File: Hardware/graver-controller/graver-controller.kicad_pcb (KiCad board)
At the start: 4 copper layers, 85 x 60 mm, 117 parts, among them J101 Power in 2p, J201 Handpiece pads 1x4, J301 USB-C, J302 SWD, J401 LCD pads 1x7, J402 Pedal pads 1x4, J403 Encoder pads 1x4, Q101 DMP6023LE, Q201 IRLR3410, Q202 SI2309CDS, Q203 BSS123, SW301 BOOT0, SW302 RESET, U101 LM5164DDAR, U102 AP2112K-3.3, U201 UCC27517DBVR, U202 TLV9062IDR, U301 STM32F411CEU6, U302 USBLC6-2SC6, U401 PESD5V0S2BT, Y301 25MHz 10pF

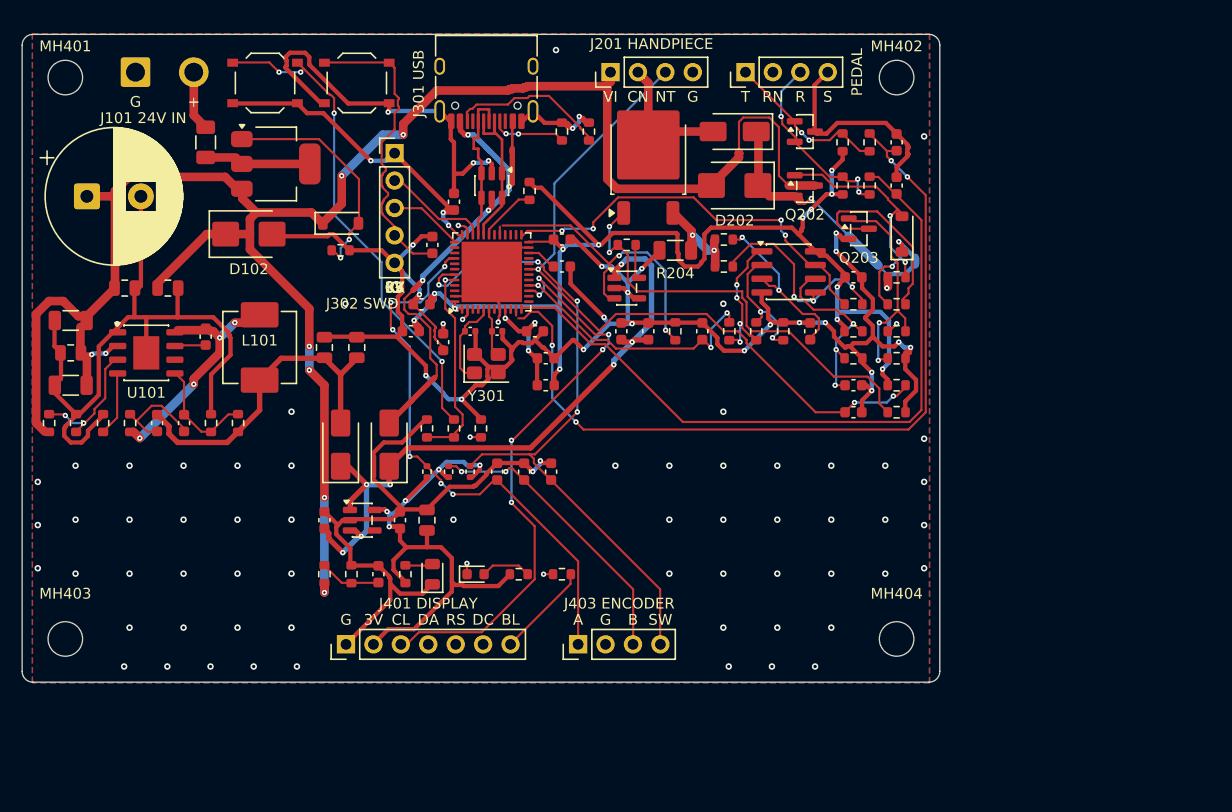
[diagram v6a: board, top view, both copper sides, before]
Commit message: pcb: ADR 0005 accepted - 4-layer board routed, DRC 0/0/0, fab set
kicad-cli DRC after a zone refill: 0 errors, 0 unconnected, 0 schematic
parity, 11 warnings (10 silk_overlap, 1 track_dangling). 85.0 x 60.0 mm.
USB pair 0.25/0.15 with 0.000 mm skew, 0 vias, F.Cu only. Two via sizes,
five track widths, In1/In2 track-free solid planes, every ADR 0003
placement rule met (tools/pcb5/check.py: 0 FAIL).

What it took beyond stage 2: a staggered stub-and-via escape for every
used QFN pin (handroute.py qfn_fan), KRT run with net class clearances and
the hand routes kept, widths snapped to the ADR set (widen.py), plane-tap
vias removed from SMD pads (postroute.py), and explicit joins for the five
pairs the router left open (joins.py: NRST under the QFN, VDDA, the LDO
input, PEDAL_TIP, a GND island). The CLAMP gate-bias branch may use signal
widths (rule area 'clamp-bias' + .kicad_dru), QFN pads need one pour spoke.

Renders in output/pcb/, JLC Gerbers/drill/BOM/CPL in fab/ with a package
convention rotation table to confirm in JLC's preview. ADR 0005 marked
Accepted with the measured numbers; HANDOFF.md points at the new pipeline.
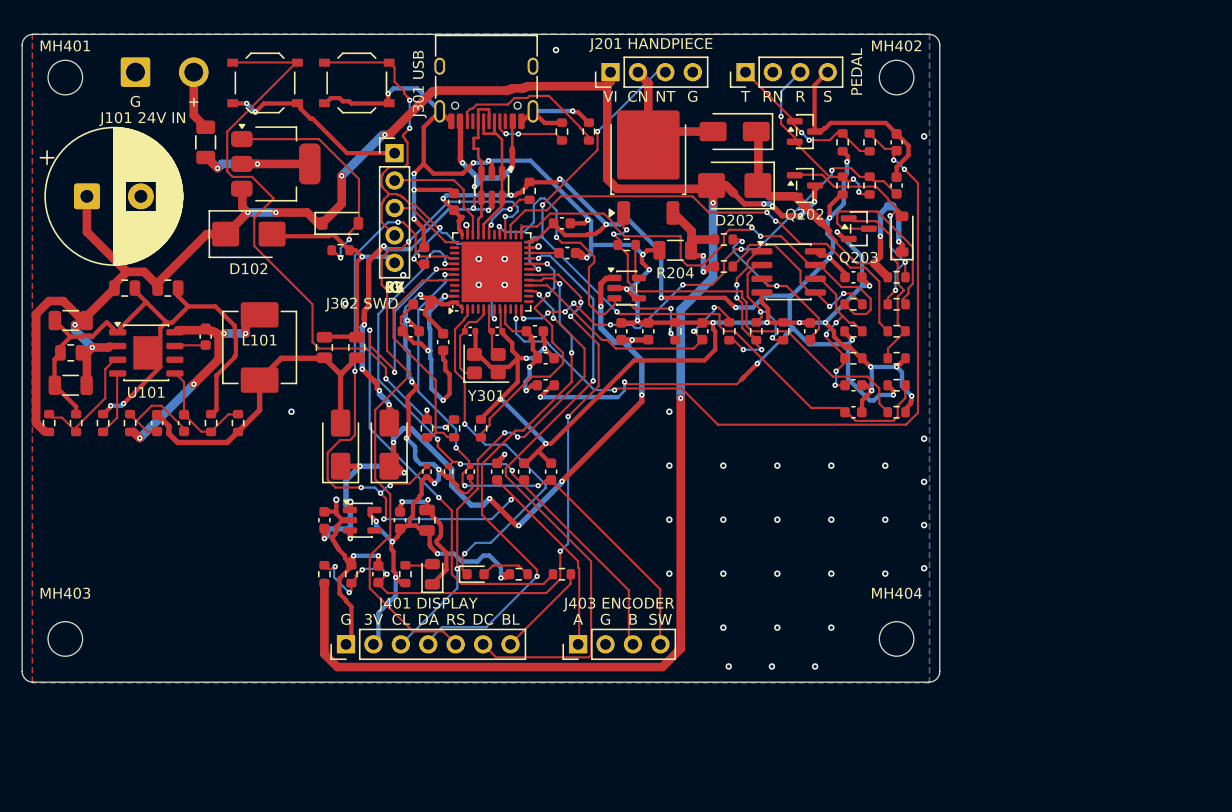
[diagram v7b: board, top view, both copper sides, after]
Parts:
- moved C302 1.50 mm to (100.0, 67.5)
- moved C308 1.35 mm to (100.5, 70.2)
- moved C309 1.25 mm to (87.2, 70.5)
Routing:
- net LCD_RST: track 0.00 -> 63.0 mm, vias 0 -> 2
- net LCD_DC: track 0.00 -> 58.0 mm, vias 0 -> 2
- net VIN_SENSE: track 5.74 -> 62.1 mm, vias 0 -> 8
- net LCD_BL: track 0.93 -> 53.4 mm, vias 1 -> 4
- net LCD_MOSI: track 0.00 -> 49.2 mm, vias 0 -> 3
- net DECAY_SLOW: track 1.11 -> 44.2 mm, vias 1 -> 2
- net +3V3: track 190.8 -> 223.6 mm, vias 22 -> 27
- net LED_STAT: track 2.19 -> 33.8 mm
- net ENC_A: track 51.1 -> 79.5 mm, vias 6 -> 7
- net VIN: track 184.7 -> 212.9 mm, vias 8 -> 12
- net ENC_B: track 27.2 -> 53.8 mm, vias 2 -> 4
- net Net-(U301-PB2): track 1.03 -> 23.8 mm, vias 1 -> 2
- net NRST: track 28.7 -> 50.7 mm, vias 0 -> 5
- net PEDAL_RING: track 65.9 -> 45.0 mm, vias 0 -> 8
- net GND: track 382.7 -> 368.9 mm, vias 90 -> 77
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
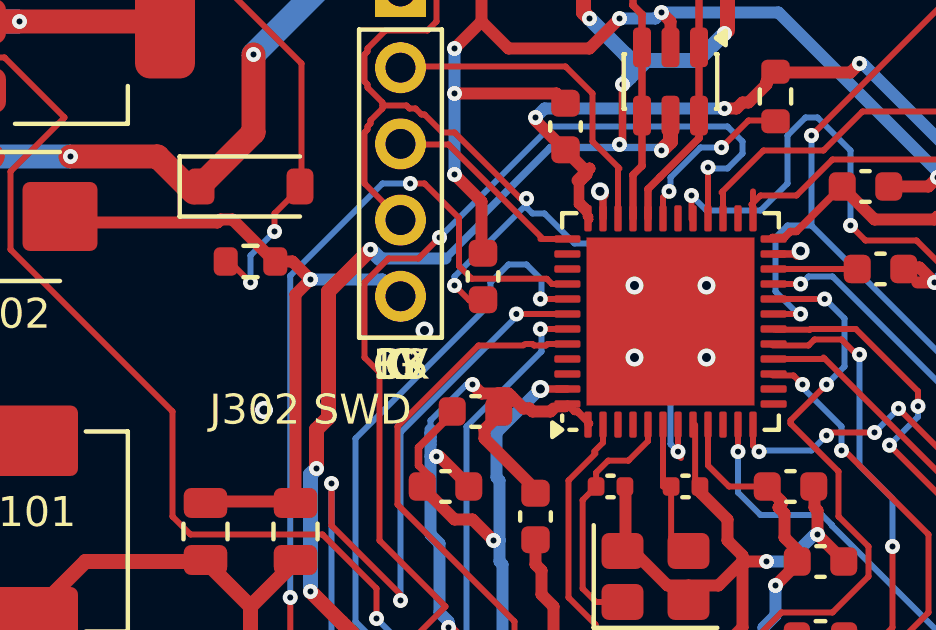
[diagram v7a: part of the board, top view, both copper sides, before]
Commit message: pcb: ADR 0005 - no DRC warnings left
The ten silk_overlap warnings were J302's five pin legends stacked on one
point by connlabels (vertical header inside the board): no legends there.
The track_dangling warning was pin 25's fan stub after its unused via was
pruned: pruned. Renders and fab set regenerated from the final board.
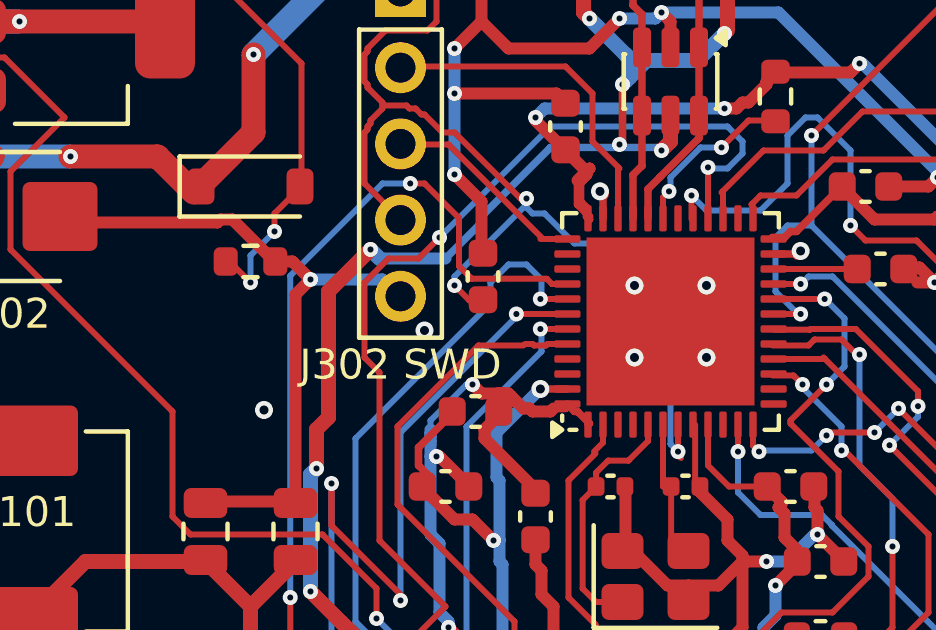
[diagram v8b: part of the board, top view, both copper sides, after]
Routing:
- net OC_TRIP: track 45.0 -> 44.1 mm
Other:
- board text removed: "CK"
- board text removed: "IO"
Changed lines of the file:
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@@
 		)
 	)
-	(gr_text "J302 SWD"
-		(at 81.5 74.94 0)
-		(layer "F.SilkS")
-		(effects
-			(font
-				(size 1 1)
-				(thickness 0.15)
-			)
-		)
-	)
 	(gr_text "3V"
 		(at 82.54 104.22 0)
@@
 		)
 	)
-	(gr_text "3V"
-		(at 84.5 73.44 0)
-		(layer "F.SilkS")
-		(effects
-			(font
-				(size 1 1)
-				(thickness 0.15)
-			)
-		)
-	)
-	(gr_text "CK"
-		(at 84.5 73.44 0)
-		(layer "F.SilkS")
-		(effects
-			(font
-				(size 1 1)
-				(thickness 0.15)
-			)
-		)
-	)
-	(gr_text "G"
-		(at 84.5 73.44 0)
-		(layer "F.SilkS")
-		(effects
-			(font
-				(size 1 1)
-				(thickness 0.15)
-			)
-		)
-	)
-	(gr_text "IO"
-		(at 84.5 73.44 0)
-		(layer "F.SilkS")
-		(effects
-			(font
-				(size 1 1)
-				(thickness 0.15)
-			)
-		)
-	)
-	(gr_text "RS"
+	(gr_text "J302 SWD"
 		(at 84.5 73.44 0)
 		(layer "F.SilkS")
@@
 	)
 	(segment
-		(start 96.25 68.5625)
-		(end 96.25 67.6625)
-		(width 0.2)
-		(layer "F.Cu")
-		(net "OC_TRIP")
-	)
-	(segment
 		(start 120.3 68.7)
 		(end 123 71.4)
@@
 			"9e3e877e-13ea-405e-a7fa-3c0cabad74a9" "9f6b5983-9b52-40b2-9815-129e7caf3155"
 			"a1518a19-97e9-47f6-a7b8-6afcdb00dce2" "a1c96735-8f77-467c-95c5-6b983ba22cbf"
-			"a293dcc5-46f2-494e-b667-7541f577e142" "b0855a08-f307-470d-b8b3-4532adee7a99"
-			"b4fdde43-1263-4148-a5b9-771494bb9842" "ba024308-56b5-411c-8534-dadd91fac284"
-			"baa22414-5d6b-467c-9acf-9113dd856370" "bb6948d9-10c7-4b91-8f27-2292cc2b84f3"
-			"bb9b2ad0-82d6-4e42-92c0-dc735c98cdaa" "bc9a5249-0c5c-4327-8367-c04faaec9576"
-			"be96302b-0bc3-4ada-bd5f-5268b67a7683" "c52d5198-71a9-4c79-b7fb-1f1d8c10b971"
-			"c8134cd8-dd7e-4d68-adab-10dd1b34157c" "cca9c78e-3c9d-4ff8-9bda-f8dd2cc53793"
-			"d1dcc57d-6307-471e-8b35-d92682c32931" "dd966713-8a46-4a80-b62d-9174777652da"
-			"e69485ac-74e8-493c-9c46-e9f32467351f" "efa93646-2413-4d1a-b108-6c18f14dc84b"
-			"efe9f32b-ec48-4e98-864f-5d76983d34ea" "f31e43f3-0568-4783-b25c-f524fcd53c11"
-			"f6aba7f9-0937-4c61-b1ca-9cdb9a789296" "f765b3b8-ccc3-48c8-9da7-8335258abaac"
-			"f844b431-237b-4766-9c39-8f5716ea4d9f" "fa4e17f1-7343-4efe-87a7-68ea056203c3"
+			"b0855a08-f307-470d-b8b3-4532adee7a99" "b4fdde43-1263-4148-a5b9-771494bb9842"
+			"ba024308-56b5-411c-8534-dadd91fac284" "baa22414-5d6b-467c-9acf-9113dd856370"
+			"bb6948d9-10c7-4b91-8f27-2292cc2b84f3" "bb9b2ad0-82d6-4e42-92c0-dc735c98cdaa"
+			"bc9a5249-0c5c-4327-8367-c04faaec9576" "be96302b-0bc3-4ada-bd5f-5268b67a7683"
+			"c52d5198-71a9-4c79-b7fb-1f1d8c10b971" "c8134cd8-dd7e-4d68-adab-10dd1b34157c"
+			"cca9c78e-3c9d-4ff8-9bda-f8dd2cc53793" "d1dcc57d-6307-471e-8b35-d92682c32931"
+			"dd966713-8a46-4a80-b62d-9174777652da" "e69485ac-74e8-493c-9c46-e9f32467351f"
+			"efa93646-2413-4d1a-b108-6c18f14dc84b" "efe9f32b-ec48-4e98-864f-5d76983d34ea"
+			"f31e43f3-0568-4783-b25c-f524fcd53c11" "f6aba7f9-0937-4c61-b1ca-9cdb9a789296"
+			"f765b3b8-ccc3-48c8-9da7-8335258abaac" "f844b431-237b-4766-9c39-8f5716ea4d9f"
+			"fa4e17f1-7343-4efe-87a7-68ea056203c3"
 		)
 	)
@@
 	)
 	(group "conn-labels"
-		(members "0540a1c7-be3b-4404-a8ca-9011a8966fe2" "0a0b6281-2fbf-487d-82c5-fb42da8c603b"
-			"14594305-c90d-40fe-9607-63d5f8763e82" "1c0b0fde-8c09-49ce-95c0-cca85be708f3"
-			"21db45ca-7014-406f-a247-8290c9308301" "27c188e9-88b9-4daa-aac7-cc613bb7ad0f"
-			"2bd23e9e-e481-4c20-89d2-5ec7e4e55d4a" "2c28228d-b109-413c-81b8-612b3b0addb8"
-			"34b773df-818c-4ae8-ad58-ebf10bc8a5de" "3a895779-ed61-4dcb-9713-8de25a4e1560"
-			"436cc31a-e032-4b0b-b7e3-2f13809efea0" "56d755f6-ae49-4e29-ace1-4d24229b1bd9"
-			"5d5da6dc-075f-4118-b324-ef6f62d58e30" "5e1cb7f3-c1fb-4be5-988d-166d0be814b8"
-			"6d5a6e12-d6ec-4d2a-bada-2355491ff64c" "7166d6de-fd10-4054-850b-122b30a2da69"
-			"77a8772f-a100-4118-9718-1dce90eabf68" "7a40ccb2-b6dd-4fd3-8bcd-816f79ddd39f"
-			"80b1d0c0-7474-4dd1-be60-7b8300e0d12a" "85f4def3-98cd-4cd3-9ac2-39343f14c941"
-			"928a6684-5017-4038-837f-9656f69117a8" "9381c4af-c51c-4dfa-89d2-bf4ea3c9880a"
-			"981433c8-3099-4673-a9b5-e5aaa410a1d0" "98171071-4e7f-47eb-ab0b-2fb958009c07"
-			"9971b0bb-2345-4e45-a042-bd4783abb2ed" "ac13a6b2-f4cd-4add-9302-4c78ab6cf480"
-			"ae971cb1-6ed6-4782-9b09-d84dfa1a32d3" "dc110d78-8625-472a-8103-bfcb484cf571"
-			"e09a122e-4e81-4fec-95a4-5416b7f9c32c" "e3ea2df2-3472-4804-974c-22b0d39895e2"
-			"ec2c0762-4379-4f94-ba65-fa9b1950ecd9" "f1b9fdeb-8be8-43f9-91a8-821f323b0865"
-			"fc1118ec-302d-4852-a994-c900cc2e80c4"
+		(members "1309783c-3ccd-4316-aa36-28371f4a7342" "15c77bd0-a77f-4200-a74e-aec9621d8cb9"
+			"15e35d49-98ca-425c-a25b-4e461170dd6d" "169b1018-2b86-48bf-a1c6-677db06e8727"
+			"2aae166e-5869-4c00-8574-01ef25b6acf0" "36074e6c-c555-4613-a309-6ad09ac9e3eb"
+			"37c604f2-4c3f-42c1-aea2-2e74f37239fb" "3b2e0640-6ec6-48b2-a86c-841b505a5eb6"
+			"3ce701f9-5fbd-42c4-b9a8-b0065656b49e" "4264ca45-0caf-482d-941a-15fb865ff2fe"
+			"4a02d5da-9289-451d-bf28-0e5ab5a9a25f" "58a27364-1a7b-437c-b70c-770a67088802"
+			"59f25965-5235-4995-bb29-abe65ea07bc7" "5bbb26c5-285c-4bba-940a-0c5c41959ad8"
+			"5dd35695-5ef5-4a57-a580-ab5cb7b21442" "6b857023-87fd-41ff-8b92-51cc8aa0f9a5"
+			"83a806b1-e41d-4e31-a117-110caa7463a8" "8655a90c-d2e9-4be3-9cb1-8ce737d2bf6d"
+			"89446d23-42b9-4232-a21d-30c69e64ac63" "8c5c6b07-695f-43c3-be8a-0fccd88fef26"
+			"a0e84ed8-5cef-4738-ae37-0c1fb0fa29df" "a5abba68-365f-4396-9a67-8d7edd04f579"
+			"b8ca1b04-bd59-4f05-92f9-ae80dd200e39" "c26a9923-3691-49d5-a1a0-2884c31a4a68"
+			"c7285414-eb84-4ca4-b624-8fd0b18f7dbc" "cb4b1f0b-2dfc-43b6-9cd5-f19db812052a"
+			"d6389e11-1dc1-4104-91a1-dc7fde6235ed" "fe711f22-a1b7-4721-ae2e-b0785f642aa5"
 		)
 	)
